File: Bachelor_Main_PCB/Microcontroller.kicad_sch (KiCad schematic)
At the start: 43 parts, among them J3 M20-9990245, J4 M20-9990245, J5 M20-9990245, J6 Conn_01x07_Pin, U3 STM32H7A3ZITxQ, U4 USB3320C-EZK-TR, Y1 SG-210STF 24Mhz, Y2 ECS-327TXO-33-TR

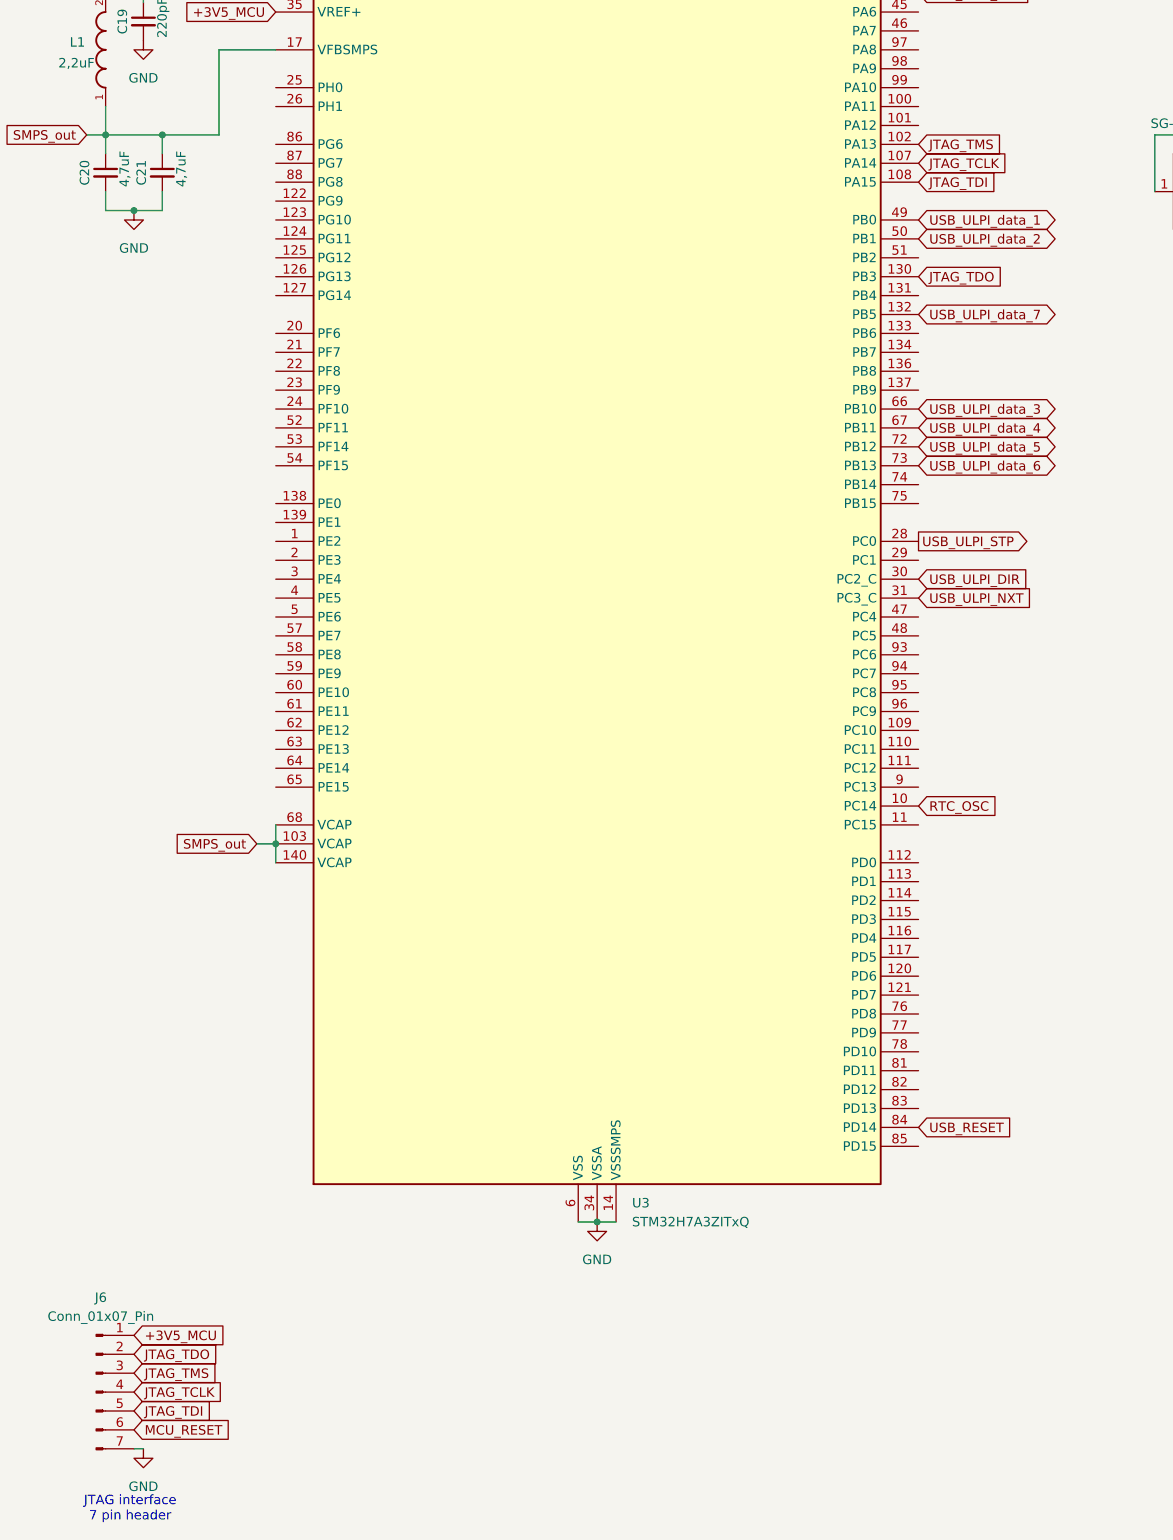
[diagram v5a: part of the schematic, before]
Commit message: Renamed JTAG_ pins to DEBUG_
Due to it being both JTAG and SWD (serial wire debug)
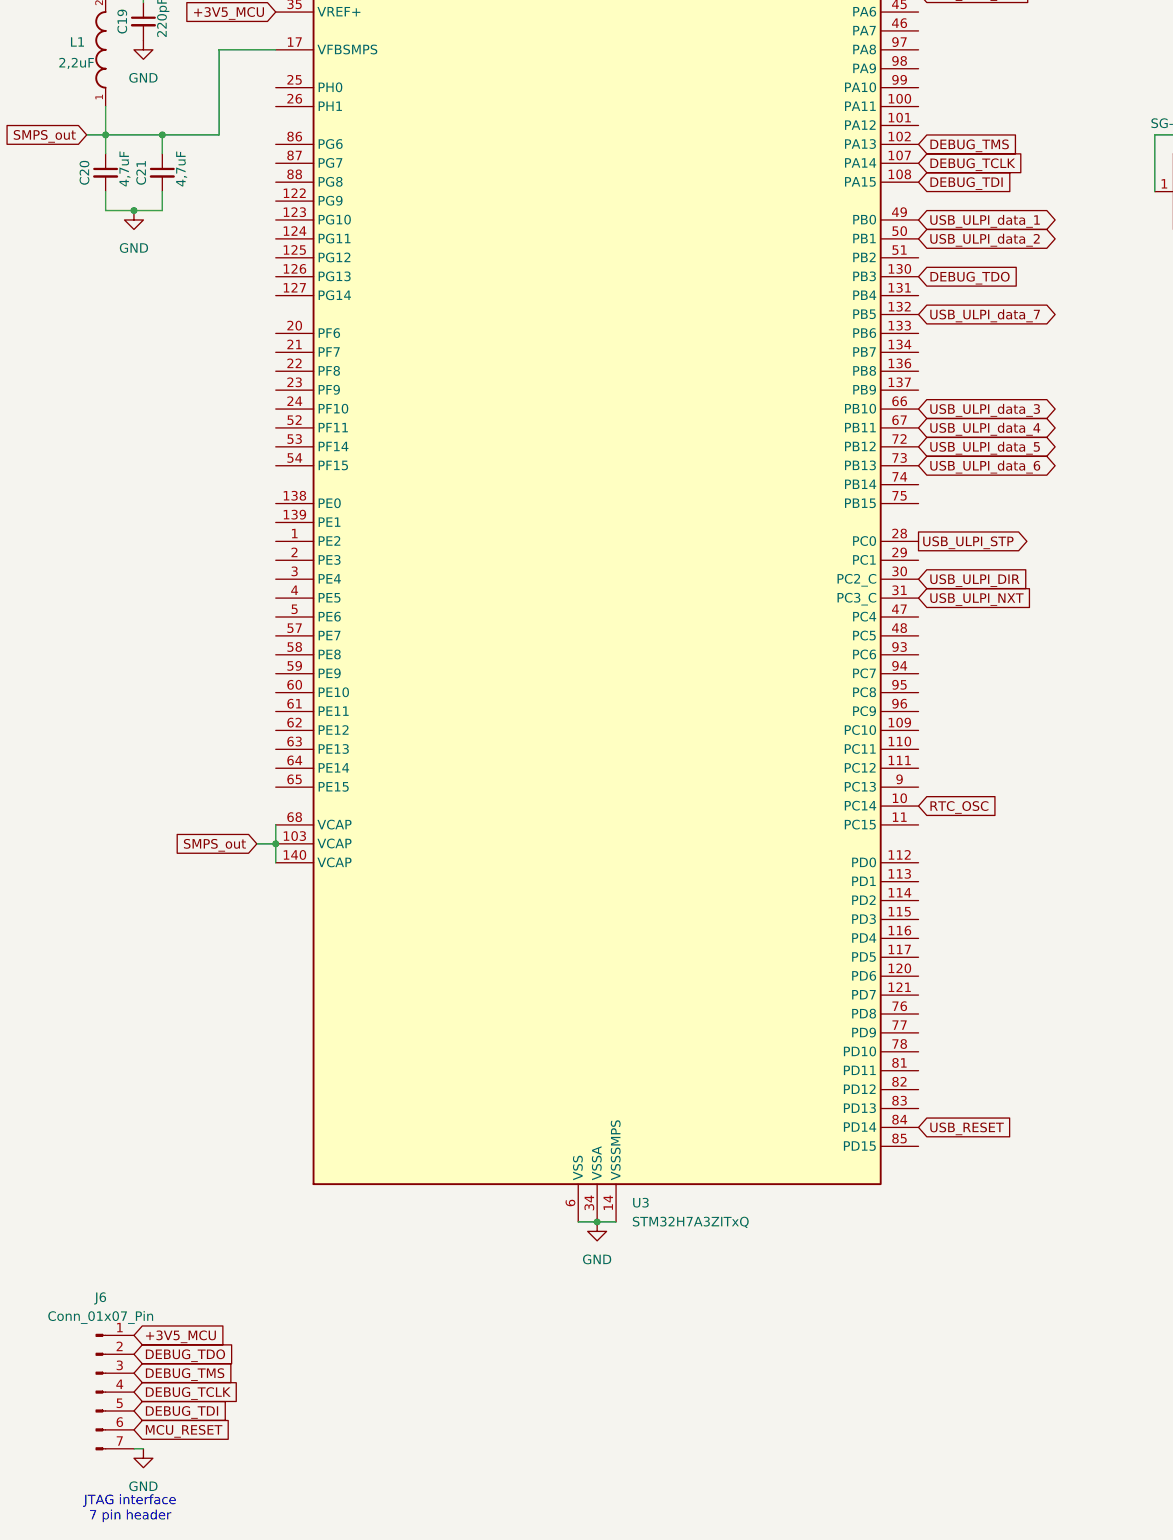
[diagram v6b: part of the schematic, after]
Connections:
- net JTAG_TCLK renamed DEBUG_TCLK
- net JTAG_TDI renamed DEBUG_TDI
- net JTAG_TDO renamed DEBUG_TDO
- net JTAG_TMS renamed DEBUG_TMS

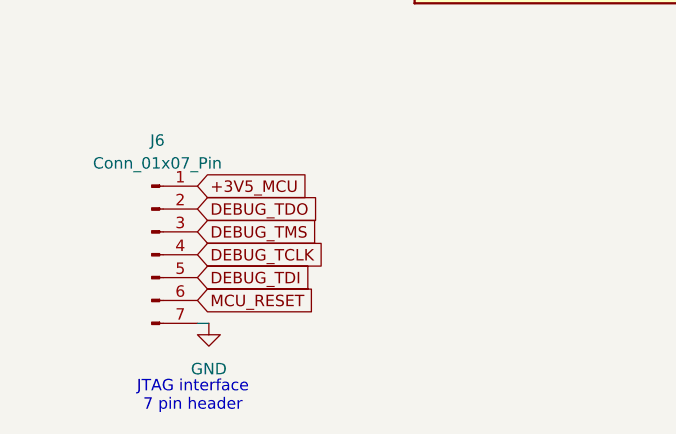
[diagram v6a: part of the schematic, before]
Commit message: More concise labeling of DEBUG pins
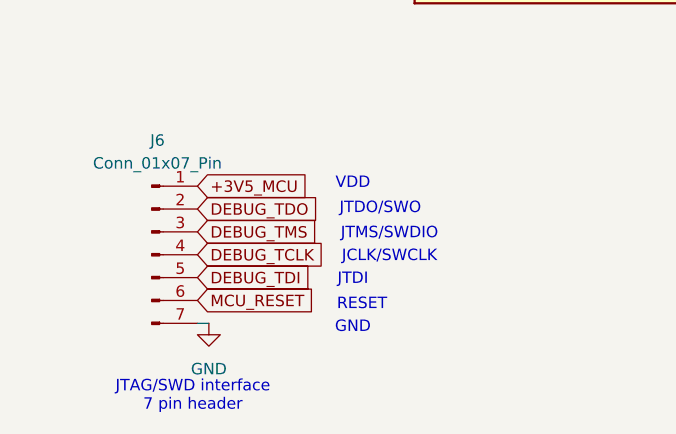
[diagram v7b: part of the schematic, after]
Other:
- note added: "GND"
- note added: "JCLK/SWCLK"
- note added: "JTAG/SWD interface 7 pin header"
- note added: "JTDI"
- note added: "JTDO/SWO"
- note added: "JTMS/SWDIO"
- note added: "RESET"
- note added: "VDD"
- note removed: "JTAG interface 7 pin header"

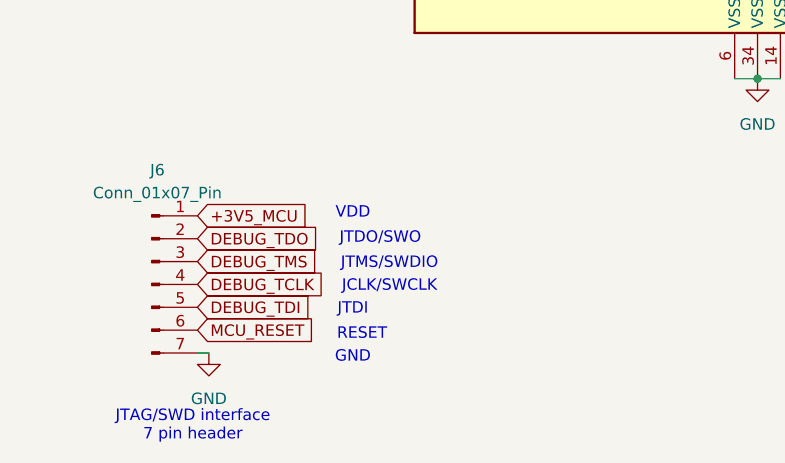
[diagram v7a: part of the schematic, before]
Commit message: MODEM power connections
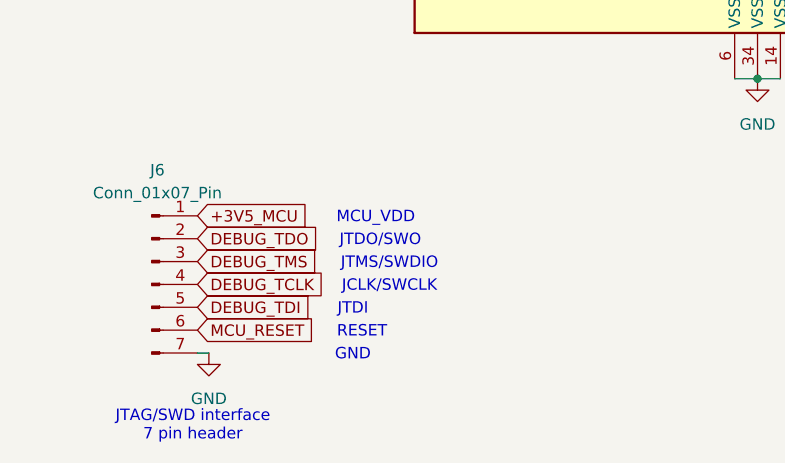
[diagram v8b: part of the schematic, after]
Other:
- note added: "MCU_VDD"
- note removed: "VDD"
